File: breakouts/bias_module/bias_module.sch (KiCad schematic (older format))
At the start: 8 parts, among them P101 CONN_01X02, U101 CONN_SMA, U102 CONN_SMA

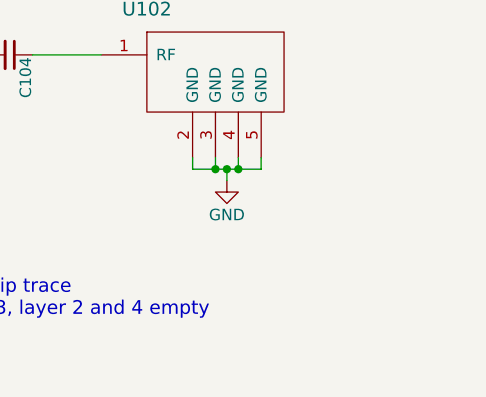
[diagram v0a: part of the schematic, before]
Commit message: finished bias module, modified mixer, splitter, and switch sma connector footprints
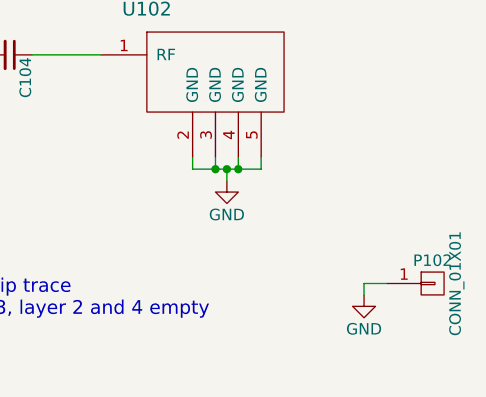
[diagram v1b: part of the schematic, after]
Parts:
- added P102: CONN_01X01, vna_footprints:BMI-S-103-NOSIDES, symbol CONN_01X01
- U101, U102: footprint (none) -> vna_footprints:732511150_sma_thin
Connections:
- net GND: now also P102.1 (P1)
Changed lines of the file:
@@
 LIBS:valves
 LIBS:conn_sma
+LIBS:conn_sma_2gnd
 LIBS:bias_module-cache
 EELAYER 25 0
@@
 $EndDescr
 $Comp
-L CONN_SMA U102
-U 1 1 57614536
-P 6450 2900
-F 0 "U102" H 6100 3100 60  0000 C CNN
-F 1 "CONN_SMA" H 6300 3250 60  0000 C CNN
-F 2 "" H 6450 2900 60  0001 C CNN
-F 3 "" H 6450 2900 60  0000 C CNN
-	1    6450 2900
-	1    0    0    -1
-$EndComp
-$Comp
-L CONN_SMA U101
-U 1 1 57614580
-P 4350 2900
-F 0 "U101" H 4000 3100 60  0000 C CNN
-F 1 "CONN_SMA" H 4200 3250 60  0000 C CNN
-F 2 "" H 4350 2900 60  0001 C CNN
-F 3 "" H 4350 2900 60  0000 C CNN
-	1    4350 2900
-	-1   0    0    -1
-$EndComp
-$Comp
 L GND #PWR01
 U 1 1 57614629
@@
 	1    0    0    -1
 $EndComp
-Wire Wire Line
-	4200 3350 4200 3400
-Wire Wire Line
-	4200 3400 4500 3400
-Wire Wire Line
-	4500 3400 4500 3350
-Wire Wire Line
-	4400 3350 4400 3400
-Connection ~ 4400 3400
-Wire Wire Line
-	4300 3350 4300 3400
-Connection ~ 4300 3400
-Wire Wire Line
-	4350 3450 4350 3400
-Connection ~ 4350 3400
 $Comp
 L GND #PWR02
@@
 	1    0    0    -1
 $EndComp
-Wire Wire Line
-	6300 3350 6300 3400
-Wire Wire Line
-	6300 3400 6600 3400
-Wire Wire Line
-	6600 3400 6600 3350
-Wire Wire Line
-	6500 3350 6500 3400
-Connection ~ 6500 3400
-Wire Wire Line
-	6400 3350 6400 3400
-Connection ~ 6400 3400
-Wire Wire Line
-	6450 3450 6450 3400
-Connection ~ 6450 3400
 $Comp
 L C_Small C104
@@
 	-1   0    0    1
 $EndComp
-Wire Wire Line
-	4900 2900 5400 2900
-Wire Wire Line
-	5150 2650 5150 2900
-Connection ~ 5150 2900
-Wire Wire Line
-	5600 2900 5900 2900
 $Comp
 L C_Small C102
@@
 	1    0    0    -1
 $EndComp
-Wire Wire Line
-	5150 1700 5150 2450
-Wire Wire Line
-	4900 1950 4900 2050
-Wire Wire Line
-	4550 1950 4550 2050
-Wire Wire Line
-	4200 1950 5150 1950
-Connection ~ 4900 1950
 $Comp
 L GND #PWR03
@@
 	1    0    0    -1
 $EndComp
-Wire Wire Line
-	4900 2300 4900 2250
-Wire Wire Line
-	4550 2300 4550 2250
 $Comp
 L GND #PWR05
@@
 	0    -1   -1   0
 $EndComp
-Connection ~ 5150 1950
-Wire Wire Line
-	5250 1700 5250 1850
-Wire Wire Line
-	5250 1850 5400 1850
-Wire Wire Line
-	5400 1850 5400 1950
 $Comp
 L C_Small C101
@@
 	1    0    0    -1
 $EndComp
-Wire Wire Line
-	4200 2300 4200 2250
-Wire Wire Line
-	4200 1950 4200 2050
-Connection ~ 4550 1950
 Text Notes 4500 4050 0    60   ~ 0
 2.75 mm wide microstrip trace\nground plane on layer 3, layer 2 and 4 empty
 Text Notes 4500 4300 0    60   ~ 0
 add BMI-S-103 shield
+Wire Wire Line
+	4200 3350 4200 3400
+Wire Wire Line
+	4200 3400 4500 3400
+Wire Wire Line
+	4500 3400 4500 3350
+Wire Wire Line
+	4400 3350 4400 3400
+Connection ~ 4400 3400
+Wire Wire Line
+	4300 3350 4300 3400
+Connection ~ 4300 3400
+Wire Wire Line
+	4350 3450 4350 3400
+Connection ~ 4350 3400
+Wire Wire Line
+	6300 3350 6300 3400
+Wire Wire Line
+	6300 3400 6600 3400
+Wire Wire Line
+	6600 3400 6600 3350
+Wire Wire Line
+	6500 3350 6500 3400
+Connection ~ 6500 3400
+Wire Wire Line
+	6400 3350 6400 3400
+Connection ~ 6400 3400
+Wire Wire Line
+	6450 3450 6450 3400
+Connection ~ 6450 3400
+Wire Wire Line
+	4900 2900 5400 2900
+Wire Wire Line
+	5150 2650 5150 2900
+Connection ~ 5150 2900
+Wire Wire Line
+	5600 2900 5900 2900
+Wire Wire Line
+	5150 1700 5150 2450
+Wire Wire Line
+	4900 1950 4900 2050
+Wire Wire Line
+	4550 1950 4550 2050
+Wire Wire Line
+	4200 1950 5150 1950
+Connection ~ 4900 1950
+Wire Wire Line
+	4900 2300 4900 2250
+Wire Wire Line
+	4550 2300 4550 2250
+Connection ~ 5150 1950
+Wire Wire Line
+	5250 1700 5250 1850
+Wire Wire Line
+	5250 1850 5400 1850
+Wire Wire Line
+	5400 1850 5400 1950
+Wire Wire Line
+	4200 2300 4200 2250
+Wire Wire Line
+	4200 1950 4200 2050
+Connection ~ 4550 1950
+$Comp
+L CONN_SMA U101
+U 1 1 57614580
+P 4350 2900
+F 0 "U101" H 4000 3100 60  0000 C CNN
+F 1 "CONN_SMA" H 4200 3250 60  0000 C CNN
+F 2 "vna_footprints:732511150_sma_thin" H 4350 2900 60  0001 C CNN
+F 3 "" H 4350 2900 60  0000 C CNN
+	1    4350 2900
+	-1   0    0    -1
+$EndComp
+$Comp
+L CONN_SMA U102
+U 1 1 57614536
+P 6450 2900
+F 0 "U102" H 6100 3100 60  0000 C CNN
+F 1 "CONN_SMA" H 6300 3250 60  0000 C CNN
+F 2 "vna_footprints:732511150_sma_thin" H 6450 2900 60  0001 C CNN
+F 3 "" H 6450 2900 60  0000 C CNN
+	1    6450 2900
+	1    0    0    -1
+$EndComp
+$Comp
+L CONN_01X01 P102
+U 1 1 576CF8BB
+P 7350 3900
+F 0 "P102" H 7350 4000 50  0000 C CNN
+F 1 "CONN_01X01" V 7450 3900 50  0000 C CNN
+F 2 "vna_footprints:BMI-S-103-NOSIDES" H 7350 3900 50  0001 C CNN
+F 3 "" H 7350 3900 50  0000 C CNN
+	1    7350 3900
+	1    0    0    -1
+$EndComp
+$Comp
+L GND #PWR07
+U 1 1 576CF8E9
+P 7050 3950
+F 0 "#PWR07" H 7050 3700 50  0001 C CNN
+F 1 "GND" H 7050 3800 50  0000 C CNN
+F 2 "" H 7050 3950 50  0000 C CNN
+F 3 "" H 7050 3950 50  0000 C CNN
+	1    7050 3950
+	1    0    0    -1
+$EndComp
+Wire Wire Line
+	7150 3900 7050 3900
+Wire Wire Line
+	7050 3900 7050 3950
 $EndSCHEMATC
